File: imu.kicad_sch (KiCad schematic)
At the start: 22 parts, among them U3 IIS2MDCTR, U4 LSM6DSO32TR, U5 TMP108AIYFFR, U6 LPS25HBTR

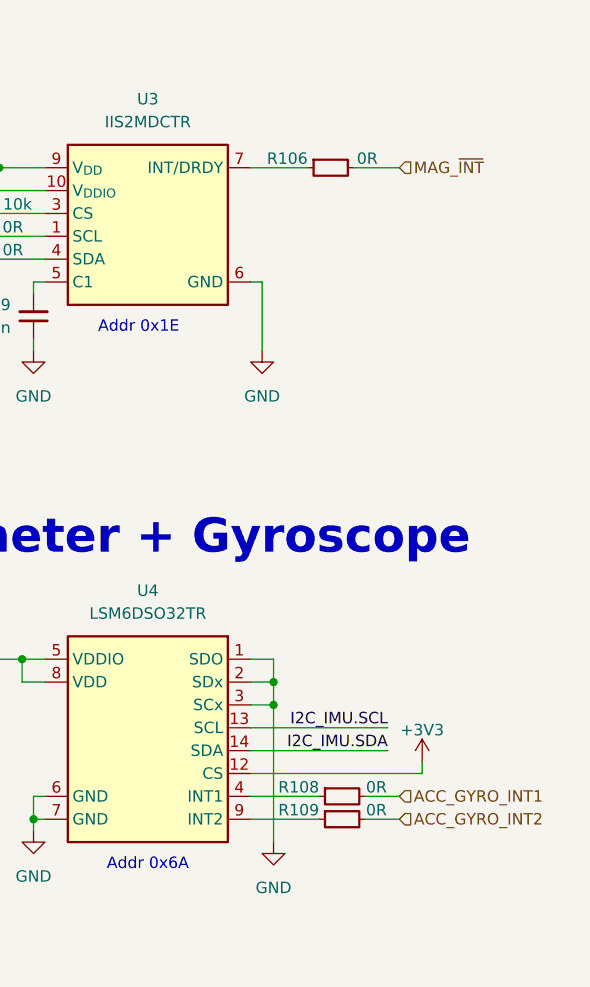
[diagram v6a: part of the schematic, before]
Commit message: [#95036] Fix hierarchical ports directions, add CAN termination jumper
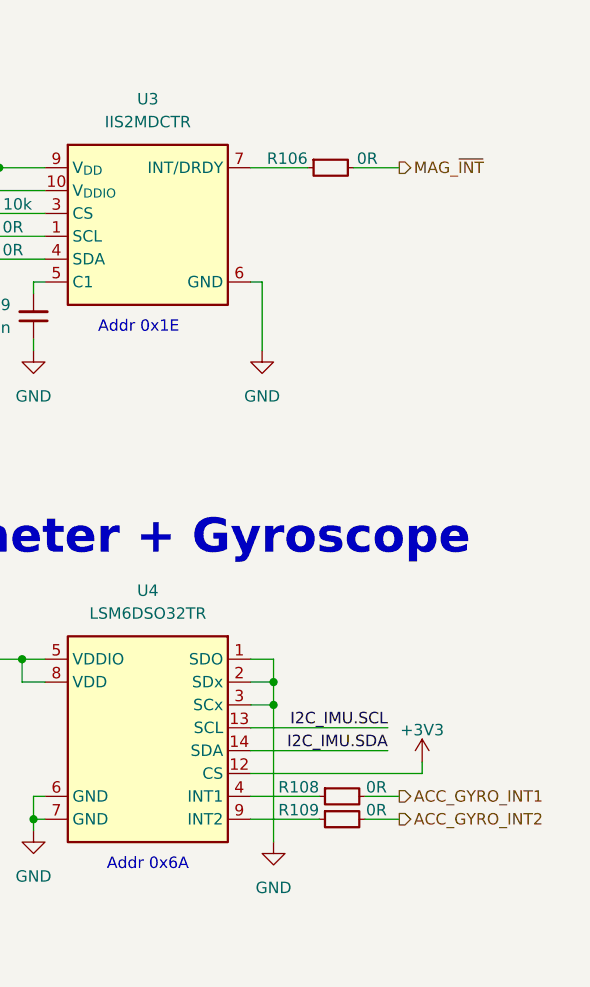
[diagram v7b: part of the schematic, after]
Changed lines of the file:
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@@
 	)
 	(hierarchical_label "ACC_GYRO_INT1"
-		(shape input)
+		(shape output)
 		(at 250.19 156.21 0)
 		(effects
@@
 	)
 	(hierarchical_label "ACC_GYRO_INT2"
-		(shape input)
+		(shape output)
 		(at 250.19 158.75 0)
 		(effects
@@
 	)
 	(hierarchical_label "MAG_~{INT}"
-		(shape input)
+		(shape output)
 		(at 250.19 86.36 0)
 		(effects
